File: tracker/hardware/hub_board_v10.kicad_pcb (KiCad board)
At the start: 2 copper layers, 72 x 80 mm, 28 parts, among them U1 U1, U2 U2, U3 U3, U5 U5, U6 U6, U7 U7

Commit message: chore(v10): routed board snapshot (10 nets, 145 tracks, 8 gates zero)
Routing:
- net /ANT1_433_TX: track 0.00 -> 84.9 mm
- net /GNSS_PPS: track 0.00 -> 65.1 mm
- net /I2C_SDA: track 0.00 -> 49.7 mm
- net /I2C_SCL: track 0.00 -> 45.4 mm
- net /USB_DP: track 0.00 -> 37.0 mm
- net /VTCXO_VNTC: track 0.00 -> 35.0 mm
- net /SPI2_MISO: track 0.00 -> 16.7 mm
- net /ANT4_GNSS_L1: track 0.00 -> 12.6 mm
- net /ANT3_2G4_RX: track 0.00 -> 10.6 mm
- net /SCAP_MID: track 0.00 -> 9.80 mm

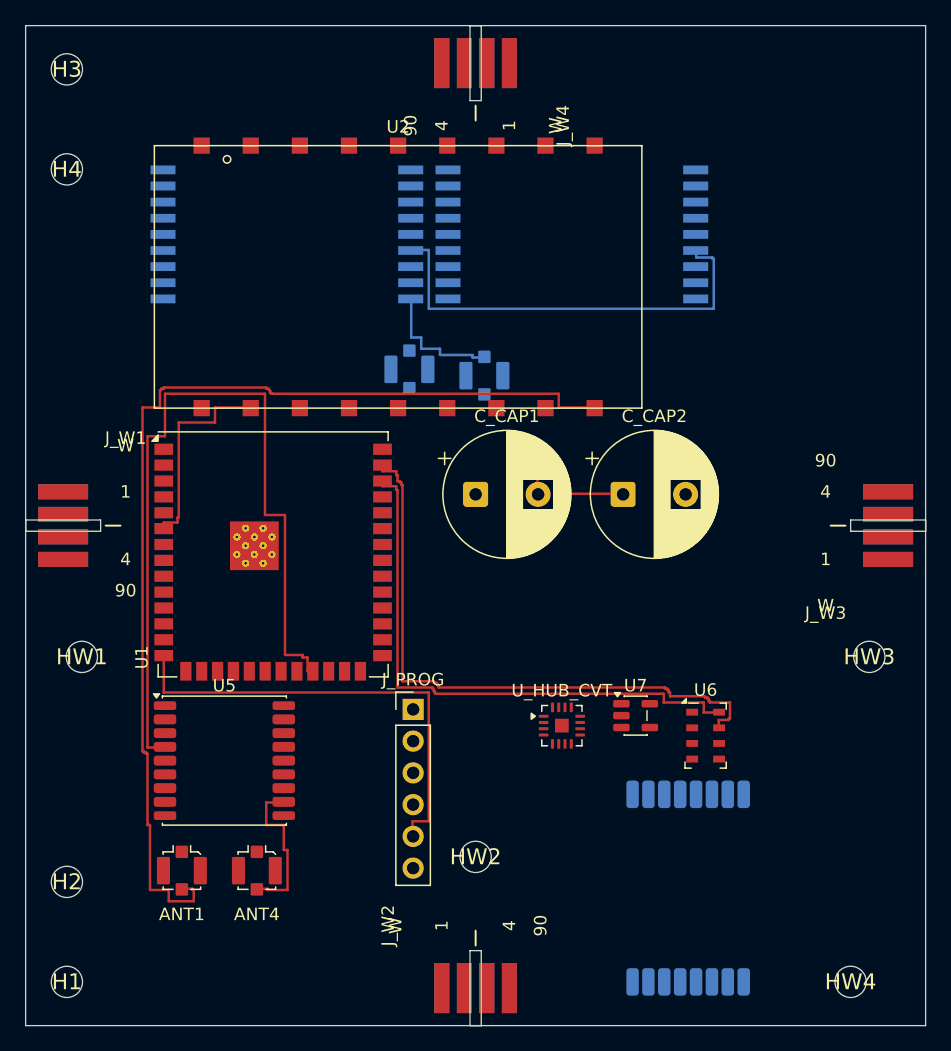
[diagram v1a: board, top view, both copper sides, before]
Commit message: feat(v10): --promote (rip-up lever) + MEASURED U1 escape capacity -- the 27 failures are LAYOUT, not routing
B31 -- added --promote: comma-separated nets forced to the FRONT of the route order. This is
rip-up-and-reroute done deterministically as a re-order: a net that failed because an earlier
net's copper blocked it gets placed first, and the blockers re-route around it.

MEASURED: promotion changed NOTHING. /SPI2_SCK, /SPI2_MOSI, /F33_CS_N, /F33_RESET_N,
/F33_BUSY, /F33_IRQ all still fail when promoted to the front. So contention for a
shared corridor is not what blocks them.

SINGLE-NET TEST -- every one of them routes ALONE:
  /SPI2_SCK routed 1 · /SPI2_MOSI routed 1 · /SPI2_MISO routed 1 · /F33_CS_N routed 1
  /F33_RESET_N routed 1 · /F33_BUSY routed 1 · /F33_IRQ routed 1        (each failed 0)

PAIRWISE / TRIO CAPACITY TEST -- this is the real result:
  {SPI2_SCK, SPI2_MOSI, SPI2_MISO}                    -> 1 routed  (of 3)
  {SPI2_SCK, SPI2_MOSI, SPI2_MISO, F33_CS_N,
   F33_RESET_N, F33_BUSY, F33_IRQ}                    -> 2 routed  (of 7)
  {SPI2_MISO, F33_BUSY}                               -> 2 routed  (of 2)  OK
  {SPI2_SCK, SPI2_MISO}                               -> 1 routed  (of 2)
  {SPI2_MOSI, SPI2_MISO}                              -> 1 routed  (of 2)

CONCLUSION: the U1 escape corridor -- the dense pin row where the SPI2 bus, the F33 control
lines and the GNSS/I2C lines all leave the ESP32 -- admits only about TWO nets of this class
at a time. Each net is individually routable; together they are over-subscribed. SPI2_MISO
wins every pairwise contest against SCK and MOSI.

This is a LAYOUT finding, not a router finding. No ordering, promotion, heuristic weight or
expansion cap changes it -- all four were swept and measured. The remaining 27 nets need one
of:
  (a) more escape room at U1's pin rows (re-place U1, or change its orientation),
  (b) immediate via escape at the U1 pads so the bus drops to B.Cu before entering the
      corridor (the corr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
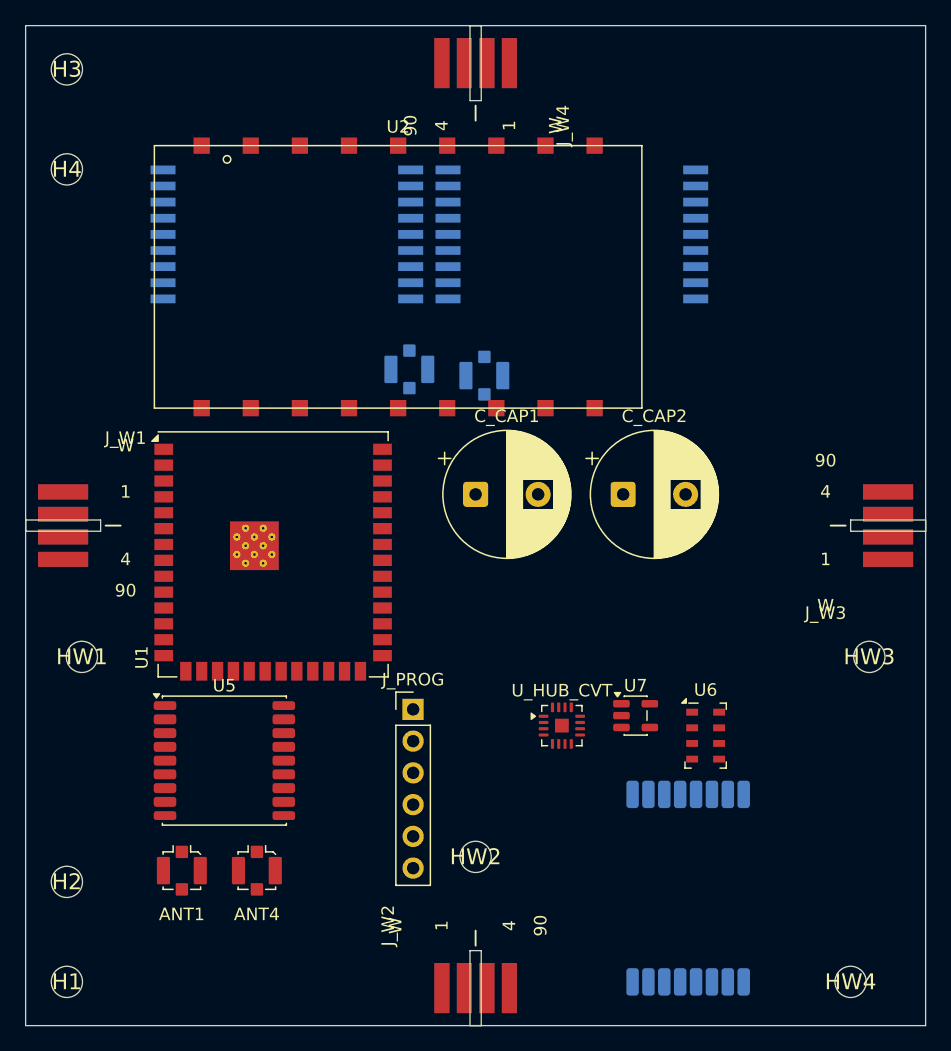
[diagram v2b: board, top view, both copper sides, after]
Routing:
- net /ANT1_433_TX: track 84.9 -> 0.00 mm
- net /GNSS_PPS: track 65.1 -> 0.00 mm
- net /I2C_SDA: track 49.7 -> 0.00 mm
- net /I2C_SCL: track 45.4 -> 0.00 mm
- net /USB_DP: track 37.0 -> 0.00 mm
- net /VTCXO_VNTC: track 35.0 -> 0.00 mm
- net /SPI2_MISO: track 16.7 -> 0.00 mm
- net /ANT4_GNSS_L1: track 12.6 -> 0.00 mm
- net /ANT3_2G4_RX: track 10.6 -> 0.00 mm
- net /SCAP_MID: track 9.80 -> 0.00 mm

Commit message: fix(v10): B32 -- via-feasibility table index bug; the router could not place ANY via
THE BUG. build_via_ok() writes a flat array of nx*ny per layer, but the store used `row[i]`
instead of `row[j*nx+i]`. Every row therefore overwrote the same nx slots, so the table held
only the LAST row's values while A* read it at `j*nx+i`. Measured consequence: via_ok reported
0.0% across the ENTIRE board, and the router placed ZERO vias -- down from 16 vias in the
pre-optimisation router.

This is the real cause of the 15 -> 10 net drop I earlier (and wrongly) attributed to the
search speed, and then to greedy ordering, and then to a layout capacity limit. It was this
one-character-class indexing error, introduced by me in B28.

WHY IT TOOK SO LONG TO FIND: my independent probe of the same rule measured 66.8% of cells
via-legal, so I concluded "the rule is fine, the table is fine" and went looking elsewhere.
The probe and the router used DIFFERENT code for the same rule -- the probe computed the disc
inline, the router read the table. Only comparing the ROUTER'S OWN TABLE to the probe's
independent result exposed it (0.0% vs 66.8%).

FIX: row[j * nx + i] = 1. Verified: via-ok 0.0% -> 64.6% per layer.

MEASURED AFTER THE FIX (full route, 93s):
  routed 11 nets (was 10): ANT4_GNSS_L1, SCAP_MID, ANT3_2G4_RX, SPI2_MISO, GNSS_PPS,
    F33_CS_N, VTCXO_VNTC, USB_DP, I2C_SCL, I2C_SDA, U3_RESET_N
  /F33_CS_N is back -- it had been failing purely because it needed a via.
  144 tracks
  all EIGHT gates 0 (geometry, holes, lane clearance, integrity, under-body, isolation,
    cross-side pad shorts, lane-vs-pad-layer)

LESSON, recorded because it cost most of a session: when an optimisation makes a previously
working feature produce ZERO results, suspect the optimisation before the domain. And when a
probe and the production code implement the same rule, compare their OUTPUTS on the same
input -- not their logic on paper.
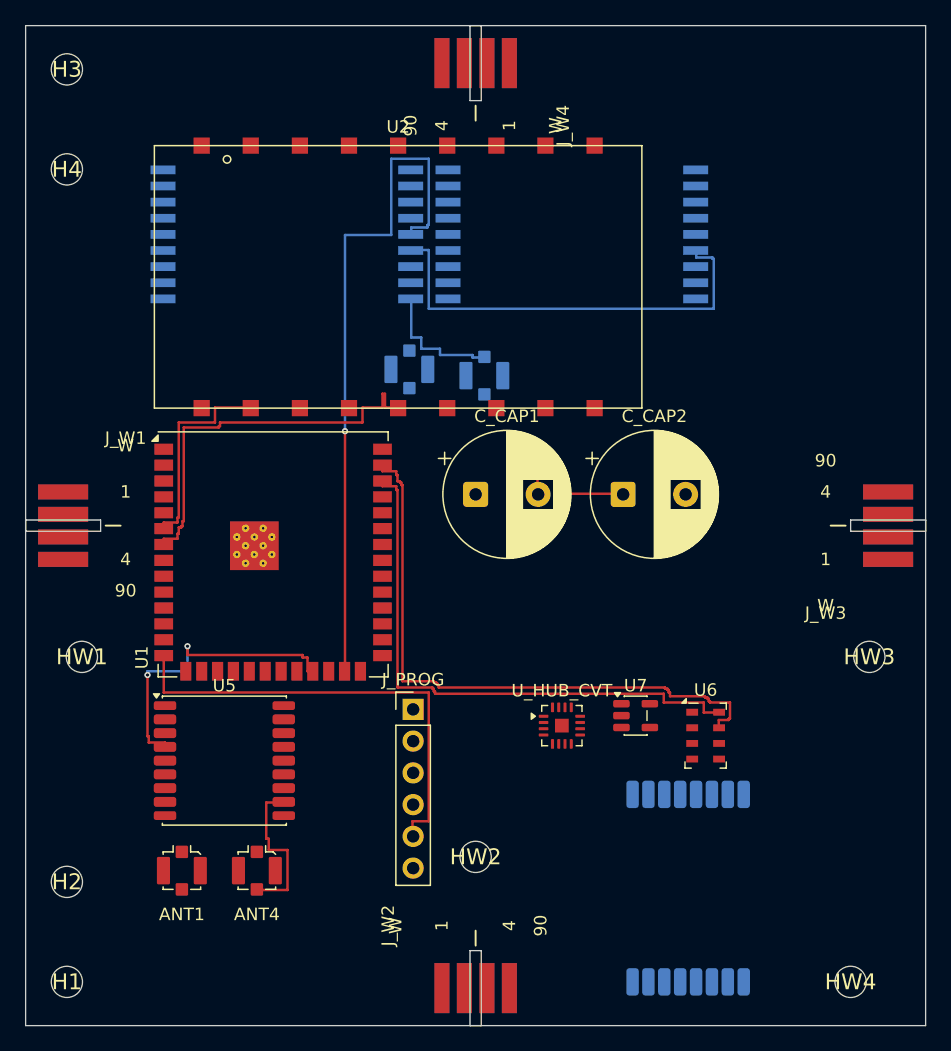
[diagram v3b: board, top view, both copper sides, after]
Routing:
- net /U3_RESET_N: track 0.00 -> 55.2 mm, vias 0 -> 1
- net /I2C_SDA: track 0.00 -> 49.7 mm
- net /I2C_SCL: track 0.00 -> 45.4 mm
- net /USB_DP: track 0.00 -> 37.0 mm
- net /VTCXO_VNTC: track 0.00 -> 35.0 mm
- net /F33_CS_N: track 0.00 -> 31.9 mm
- net /GNSS_PPS: track 0.00 -> 24.7 mm, vias 0 -> 2
- net /SPI2_MISO: track 0.00 -> 16.7 mm
- net /ANT4_GNSS_L1: track 0.00 -> 12.6 mm
- net /ANT3_2G4_RX: track 0.00 -> 10.6 mm
- net /SCAP_MID: track 0.00 -> 9.80 mm

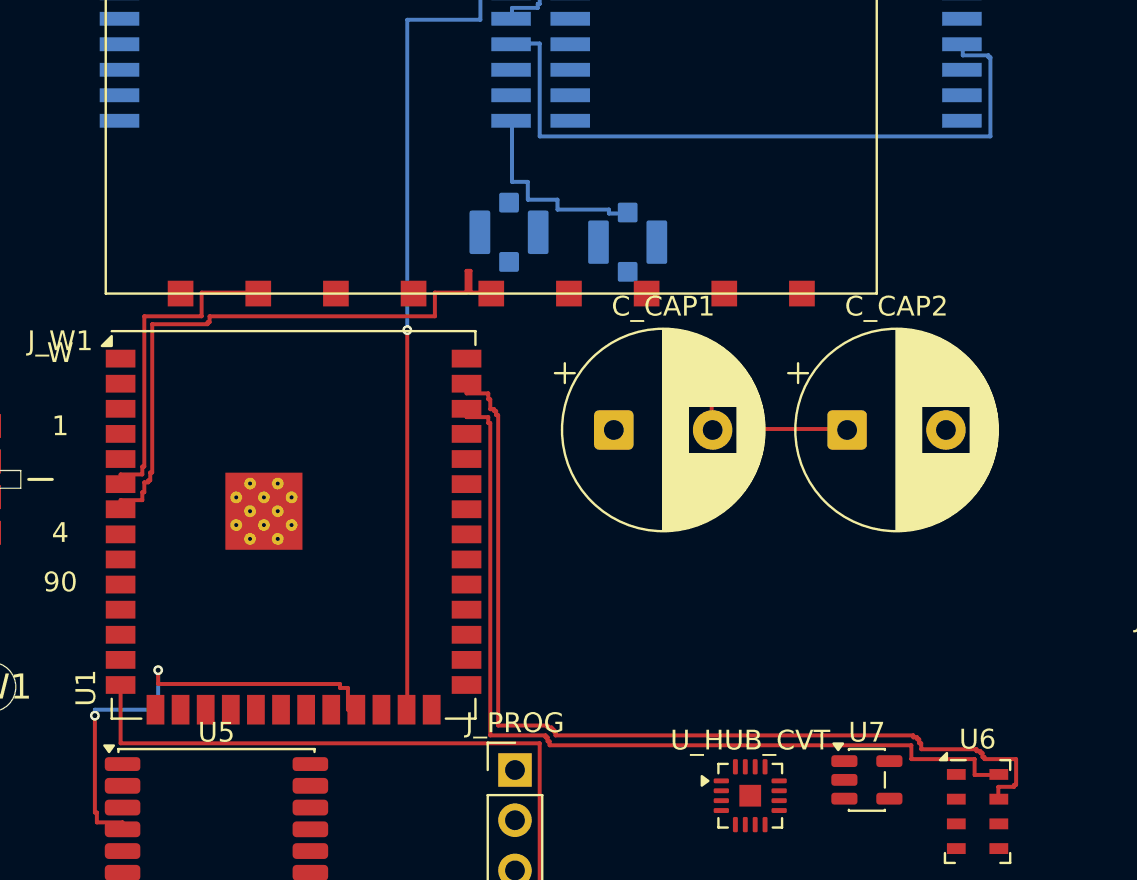
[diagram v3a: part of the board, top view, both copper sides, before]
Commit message: fix(v10): B34 -- isolation obstacle under-marked by 0.10mm; the router was throwing away valid paths
THE BUG. When a net is accepted, its copper is marked into the A* grid so later nets route
around it. The mark used `g = CLEAR + TRACK_W/2` = 0.30mm. But a grid cell is a candidate
CENTRELINE for the new track, so keeping CLEAR between copper EDGES requires

    centre-to-centre >= CLEAR + (other track's half) + (own half) = CLEAR + TRACK_W = 0.40mm

0.30mm under-marked by exactly 0.10mm. Consequence, measured directly:

    /SPI2_MISO routed first, then
    /SPI2_MOSI -> "self-check: isolation vs routed /SPI2_MISO"
    /SPI2_SCK  -> "self-check: isolation vs routed /SPI2_MISO"

i.e. A* FOUND a path and validate_plan THREW IT AWAY. That is why the SPI2 trio could never
route together regardless of ordering, promotion, heuristic weight, expansion cap or via cost
-- all five were swept and all five changed nothing, because the router was discarding its own
work at the last step. It also explains why the earlier "layout capacity" conclusion looked so
solid: the evidence was consistent, and consistently produced by this bug.

HOW IT WAS FOUND: added --append (incremental routing) so a net could be routed onto a board
that already had copper, then routed the trio ONE AT A TIME. The failure message named the
mechanism exactly. Without --append the router refuses to touch a board with existing tracks
(exit 4, my own guard), which had hidden this.

MEASURED AFTER THE FIX (full route, ~90s):
  routed 12 nets (was 11): ANT4_GNSS_L1, SCAP_MID, ANT3_2G4_RX, SPI2_MISO, GNSS_PPS,
    F33_CS_N, F33_BUSY, VTCXO_VNTC, USB_DP, I2C_SCL, I2C_SDA, U3_RESET_N
  /F33_BUSY recovered
  181 tracks
  all EIGHT gates 0

NEW FEATURE: --append. Routes onto a board that already has copper; existing tracks are loaded
as grid obstacles AND as routed copper so the isolation self-check applies to them.

CORRECTION TO THE RECORD: docs/fab/v10/ROUTING-CAPACITY-FINDING.md concluded the 27 unrouted
nets w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
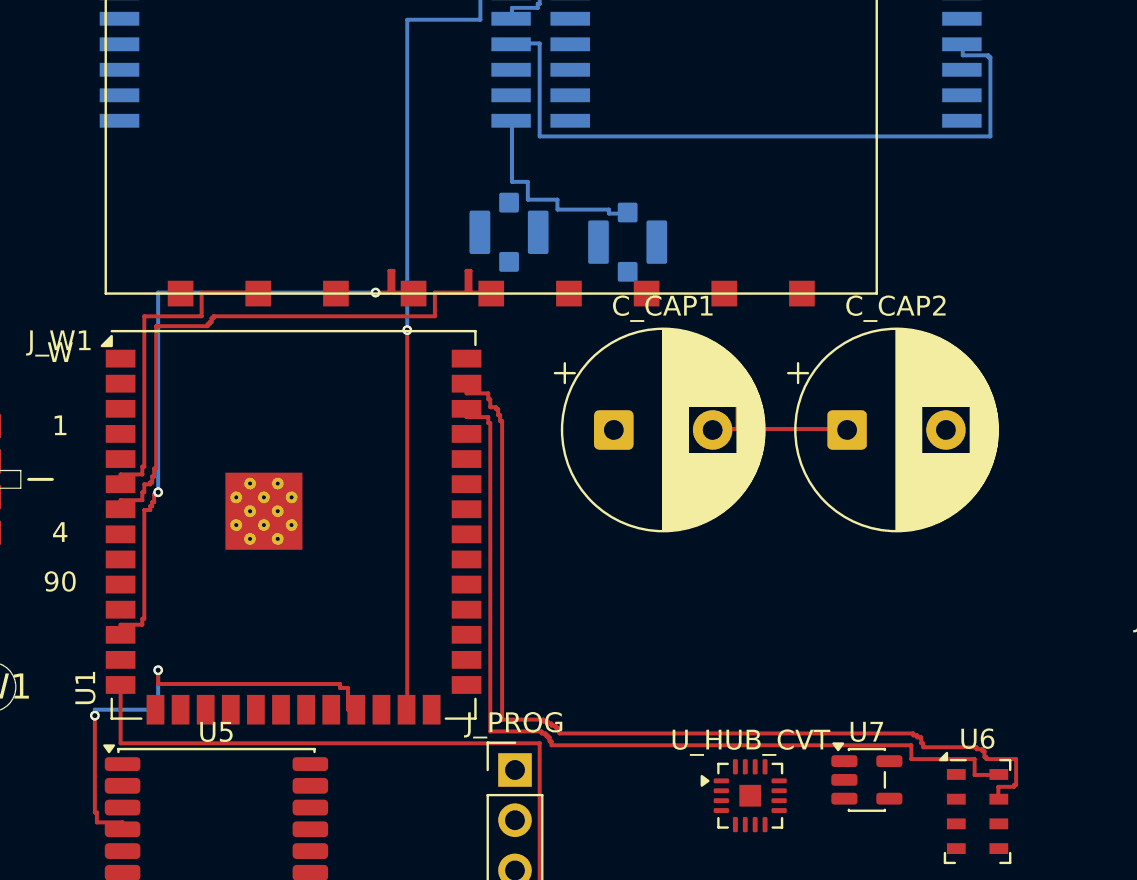
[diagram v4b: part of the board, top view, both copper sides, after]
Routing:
- net /F33_BUSY: track 0.00 -> 34.3 mm, vias 0 -> 2

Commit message: chore(v10): routed board snapshot -- 12 nets, 209 tracks, 8 gates zero (after B34)
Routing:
- net /F33_BUSY: vias 2 -> 0
